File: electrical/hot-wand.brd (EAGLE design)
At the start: 112 x 72 mm, 192 parts, among them IC1 12V R-78K12-2.0, IC2 3V3 R-78K3.3, Q1 STP19NF20, Q2 IRF510, Q3 BC846B, Q4 SIS862ADN-T1-GE3, Q5 2N7002K, Q6 DMTH64M2LPDWQ-13, Q7 SIS862ADN-T1-GE3, Q8 G3404, U1 TPS54560DDA, U2 1EDN8511BXUSA1, U3 INA138, U4 LM74700QDBVTQ1, U5 AP53781, U6 SSD1306-4PIN-0.91N-VERT, U7 STM32F030F4P6, Y1 27.12 MHz 10pF

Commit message: added test points to aid in testing, marks for solder jumpers
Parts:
- added TP1, TP2: TEST-POINT-SQ-2MM, hot-wand:PAD-SQ-2MM
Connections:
- net PWR-ATTENU: now also TP2.1
- net RF-GEN: now also TP1.1
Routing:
- net PWR-ATTENU: track 52.4 -> 55.8 mm
- net RF-GEN: track 58.3 -> 61.0 mm
- net GND: vias 651 -> 652
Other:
- board text added: "A"
- board text added: "B"
- board text added: "C"
- board text added: "D"
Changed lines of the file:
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@@
 </polygon>
 <polygon width="0.2032" layer="32">
-<vertex x="22.8" y="21.6"/>
-<vertex x="24.5" y="21.6"/>
-<vertex x="24.5" y="20.5"/>
-<vertex x="22.8" y="20.5"/>
+<vertex x="21.8" y="21.6"/>
+<vertex x="23.2" y="21.6"/>
+<vertex x="23.2" y="20.4"/>
+<vertex x="21.8" y="20.4"/>
 </polygon>
 <polygon width="0.2032" layer="32">
@@
 <vertex x="90.5" y="65.5"/>
 </polygon>
+<text x="19.2" y="29" size="0.8128" layer="22" font="vector" rot="MR0" align="center">C</text>
+<text x="20.6" y="32.9" size="0.8128" layer="22" font="vector" rot="MR0" align="center">D</text>
+<text x="25" y="20.3" size="0.8128" layer="22" font="vector" rot="MR0" align="center">A</text>
+<text x="20.8" y="21.4" size="0.8128" layer="22" font="vector" rot="MR0" align="center">B</text>
 </plain>
 <attributes>
@@
 </element>
 <element name="L3" library="hot-wand" package="IND_K16X8X6_X2" value="9uH" x="69" y="47" smashed="yes" rot="R270">
-<attribute name="NAME" x="66.9" y="46" size="0.8128" layer="25" font="vector"/>
-<attribute name="VALUE" x="71.3" y="47.9" size="0.8128" layer="27" font="vector" rot="R180"/>
+<attribute name="NAME" x="67" y="44.9" size="0.8128" layer="25" font="vector"/>
+<attribute name="VALUE" x="71.4" y="48.6" size="0.8128" layer="27" font="vector" rot="R180"/>
 <attribute name="JLC-DNP" value="1" x="69" y="47" size="1.778" layer="27" rot="R270" display="off"/>
 </element>
@@
 <attribute name="VALUE" x="40.789" y="50.66" size="0.8128" layer="27" font="vector" ratio="10"/>
 <attribute name="JLC-DNP" value="1" x="45" y="47" size="1.778" layer="27" display="off"/>
+<attribute name="NOTE" value="22 µH fitted; 33 µH original/preferred; 13 µH calculated minimum" x="45" y="47" size="1.778" layer="27" display="off"/>
 </element>
 <element name="L2" library="hot-wand" package="IND_IHLP-2525CZ_VIS-M" value="4u7 IHLP2525CZ" x="55" y="41.4" smashed="yes" rot="MR180">
@@
 <attribute name="NAME" x="92.6" y="66.1" size="0.8128" layer="26" font="fixed" rot="MR90"/>
 </element>
-<element name="FAN1" library="hot-wand" package="FAN-CONN-X4" value="FAN-CONN-X4-CONN-X4" x="23" y="27" smashed="yes" rot="R180"/>
+<element name="FAN1" library="hot-wand" package="FAN-CONN-X4" value="FAN-CONN-X4-CONN-X4" x="23" y="27" smashed="yes" rot="R180">
+<attribute name="PARTNUM" value="WM9797-ND;0470533000" x="23" y="27" size="0.8128" layer="27" font="vector" rot="R180" align="center" display="off"/>
+</element>
 <element name="SJ4" library="hot-wand" package="SJ_3" value="" x="23" y="21" smashed="yes" rot="MR0">
 <attribute name="NAME" x="22.43" y="19.73" size="0.8128" layer="26" rot="MR180"/>
@@
 <attribute name="VALUE" x="20.7" y="30.6999" size="0.02" layer="28" rot="MR90"/>
 <attribute name="VALUE" x="18.795" y="29.53" size="0.4064" layer="28" rot="MR90"/>
+</element>
+<element name="TP1" library="hot-wand" package="PAD-SQ-2MM" value="TEST-POINT-SQ-2MM" x="47.3" y="20.9" smashed="yes">
+<attribute name="NAME" x="46" y="22.3" size="0.8128" layer="25"/>
+</element>
+<element name="TP2" library="hot-wand" package="PAD-SQ-2MM" value="TEST-POINT-SQ-2MM" x="50.6" y="18.8" smashed="yes">
+<attribute name="NAME" x="50.2" y="20.2" size="0.8128" layer="25"/>
 </element>
 </elements>
@@
 <via x="70.5" y="52.1" extent="1-16" drill="0.3" shape="octagon"/>
 <via x="70.4" y="49" extent="1-16" drill="0.3" shape="octagon"/>
-<via x="75.2" y="46" extent="1-16" drill="0.3" shape="octagon"/>
 <via x="71.4" y="45" extent="1-16" drill="0.3" shape="octagon"/>
 <via x="63" y="45" extent="1-16" drill="0.3" shape="octagon"/>
 <via x="60" y="45" extent="1-16" drill="0.3" shape="octagon"/>
 <via x="67" y="49" extent="1-16" drill="0.3" shape="octagon"/>
-<via x="67.4" y="46" extent="1-16" drill="0.3" shape="octagon"/>
 <via x="67.4" y="44" extent="1-16" drill="0.3" shape="octagon"/>
 <via x="67.4" y="42" extent="1-16" drill="0.3" shape="octagon"/>
@@
 <via x="38" y="17.2" extent="1-16" drill="0.3" shape="octagon"/>
 <via x="38" y="13.8" extent="1-16" drill="0.3" shape="octagon"/>
-<via x="46.7" y="19.3" extent="1-16" drill="0.3" shape="octagon"/>
+<via x="46.2" y="19.1" extent="1-16" drill="0.3" shape="octagon"/>
 <via x="45.8" y="15.2" extent="1-16" drill="0.3" shape="octagon"/>
 <via x="45.8" y="13.8" extent="1-16" drill="0.3" shape="octagon"/>
@@
 <via x="54" y="30" extent="1-16" drill="0.3" shape="octagon"/>
 <via x="50" y="33" extent="1-16" drill="0.3" shape="octagon"/>
-<via x="44" y="36" extent="1-16" drill="0.3" shape="octagon"/>
+<via x="44" y="35.4" extent="1-16" drill="0.3" shape="octagon"/>
 <via x="44" y="34" extent="1-16" drill="0.3" shape="octagon"/>
 <via x="13" y="24" extent="1-16" drill="0.3" shape="octagon"/>
@@
 <via x="54.5" y="58" extent="1-16" drill="0.3" shape="octagon"/>
 <via x="56" y="58" extent="1-16" drill="0.3" shape="octagon"/>
-<via x="63.5" y="68.9" extent="1-16" drill="0.3" shape="octagon"/>
+<via x="63.54" y="68.9" extent="1-16" drill="0.3" shape="octagon"/>
 <contactref element="C61" pad="C"/>
 <contactref element="SJ4" pad="1"/>
@@
 <via x="26.8" y="30.1" extent="1-16" drill="0.3" shape="octagon"/>
 <via x="24.8" y="30.1" extent="1-16" drill="0.3" shape="octagon"/>
-<via x="25.8" y="20.9" extent="1-16" drill="0.3" shape="octagon"/>
+<via x="25.8" y="21" extent="1-16" drill="0.3" shape="octagon"/>
 <via x="27.2" y="22.5" extent="1-16" drill="0.3" shape="octagon"/>
 <via x="23.9" y="19.8" extent="1-16" drill="0.3" shape="octagon"/>
@@
 <via x="101" y="62.9" extent="1-16" drill="0.3" shape="octagon"/>
 <via x="101" y="59.7" extent="1-16" drill="0.3" shape="octagon"/>
+<via x="75.1" y="44.7" extent="1-16" drill="1" diameter="2" shape="octagon" alwaysstop="yes"/>
+<via x="68" y="47" extent="1-16" drill="1" diameter="2" shape="octagon" alwaysstop="yes"/>
+<via x="24.8" y="21" extent="1-16" drill="0.3" shape="octagon"/>
 </signal>
 <signal name="RF-OUT">
@@
 <wire x1="48.2" y1="27.2" x2="45.4" y2="30" width="0.2032" layer="1"/>
 <wire x1="45.4" y1="30" x2="43.1" y2="30" width="0.2032" layer="1"/>
-<wire x1="38.8" y1="48.2" x2="42.7" y2="52.1" width="0.2032" layer="1"/>
-<wire x1="42.7" y1="52.1" x2="42.7" y2="57.7" width="0.2032" layer="1"/>
+<wire x1="38.8" y1="48.4" x2="42.7" y2="52.3" width="0.2032" layer="1"/>
+<wire x1="42.7" y1="52.3" x2="42.7" y2="57.7" width="0.2032" layer="1"/>
 <wire x1="42.7" y1="57.7" x2="44" y2="59" width="0.2032" layer="1"/>
 <wire x1="44" y1="59" x2="44" y2="67.4" width="0.2032" layer="1"/>
 <via x="44" y="67.4" extent="1-16" drill="0.3" shape="octagon"/>
-<wire x1="38.8" y1="34.3" x2="38.8" y2="48.2" width="0.2032" layer="1"/>
+<wire x1="38.8" y1="34.3" x2="38.8" y2="48.4" width="0.2032" layer="1"/>
 <wire x1="38.8" y1="34.3" x2="43.1" y2="30" width="0.2032" layer="1"/>
 <wire x1="44" y1="67.4" x2="44" y2="68.9" width="0.4064" layer="16"/>
 <contactref element="R52" pad="2"/>
 <wire x1="48.2" y1="18" x2="48.2" y2="19.1" width="0.4064" layer="16"/>
+<contactref element="TP1" pad="1"/>
+<wire x1="47.3" y1="20.9" x2="48.2" y2="20.9" width="0.2032" layer="1"/>
+<wire x1="48.2" y1="20.9" x2="48.2" y2="19.1" width="0.2032" layer="1"/>
 </signal>
 <signal name="N$28">
@@
 <wire x1="49.7" y1="27.698334375" x2="46.098334375" y2="31.3" width="0.2032" layer="1"/>
 <wire x1="46.098334375" y1="31.3" x2="43.5" y2="31.3" width="0.2032" layer="1"/>
-<wire x1="39.9" y1="34.9" x2="39.9" y2="47.7" width="0.2032" layer="1"/>
-<wire x1="39.9" y1="47.7" x2="44.2" y2="52" width="0.2032" layer="1"/>
-<via x="44.2" y="52" extent="1-16" drill="0.3" shape="octagon"/>
-<wire x1="44.2" y1="52" x2="45.35" y2="52" width="0.4064" layer="16"/>
-<wire x1="45.35" y1="52" x2="46.6" y2="53.25" width="0.4064" layer="16"/>
+<wire x1="39.9" y1="34.9" x2="39.9" y2="47.8" width="0.2032" layer="1"/>
+<wire x1="39.9" y1="47.8" x2="44.2" y2="52.1" width="0.2032" layer="1"/>
+<via x="44.2" y="52.1" extent="1-16" drill="0.3" shape="octagon"/>
+<wire x1="44.2" y1="52.1" x2="45.45" y2="52.1" width="0.4064" layer="16"/>
+<wire x1="45.45" y1="52.1" x2="46.6" y2="53.25" width="0.4064" layer="16"/>
 <via x="49.7" y="16.4" extent="1-16" drill="0.3" shape="octagon"/>
 <wire x1="39.9" y1="34.9" x2="43.5" y2="31.3" width="0.2032" layer="1"/>
+<contactref element="TP2" pad="1"/>
+<wire x1="50.6" y1="18.8" x2="49.7" y2="18.8" width="0.2032" layer="1"/>
+<wire x1="49.7" y1="18.8" x2="49.7" y2="16.4" width="0.2032" layer="1"/>
 </signal>
 <signal name="12V-2">

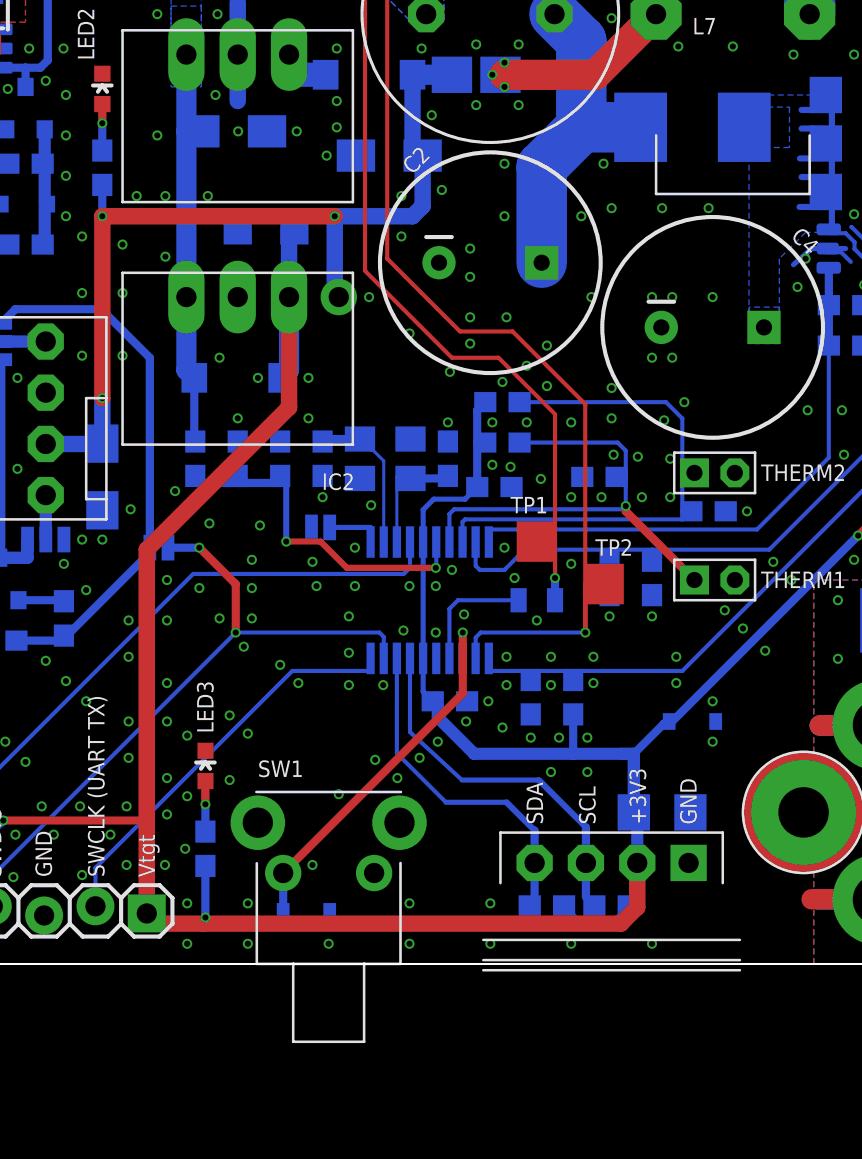
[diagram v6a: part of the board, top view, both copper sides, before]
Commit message: moved the oled, 3.3V buck converter footprint fixed
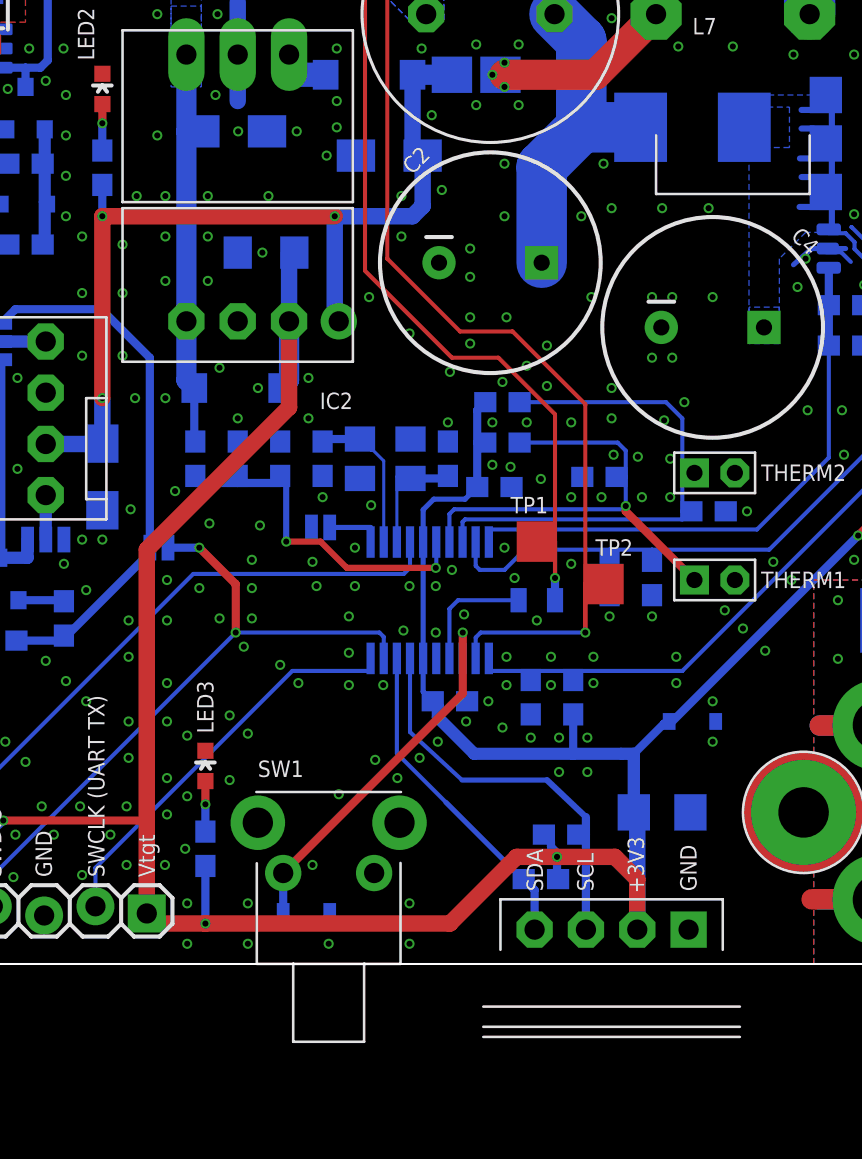
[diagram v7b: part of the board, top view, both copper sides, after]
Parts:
- IC1: device hot-wand:TO220-BUCK -> hot-wand:TO220-BUCK-12V
- IC2: device hot-wand:TO220-BUCK -> hot-wand:TO220-BUCK-3.3V
- moved R36 4.30 mm to (48.5, 6.40), turned to 0 degrees
- moved U6 3.30 mm to (51.0, 1.70)
- moved R35 1.33 mm to (47.5, 4.20)
- moved IC2 1.20 mm to (32.5, 31.8)
- moved C45 1.20 mm to (33.9, 35.2)
- moved D11 0.50 mm to (32.5, 28.5)
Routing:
- net SCL: track 18.3 -> 20.0 mm
- net +12V: track 44.7 -> 45.9 mm
- net SDA: track 17.0 -> 16.3 mm
- net 3.3V: track 140.9 -> 140.4 mm, vias 3 -> 4
- net GND: vias 652 -> 655

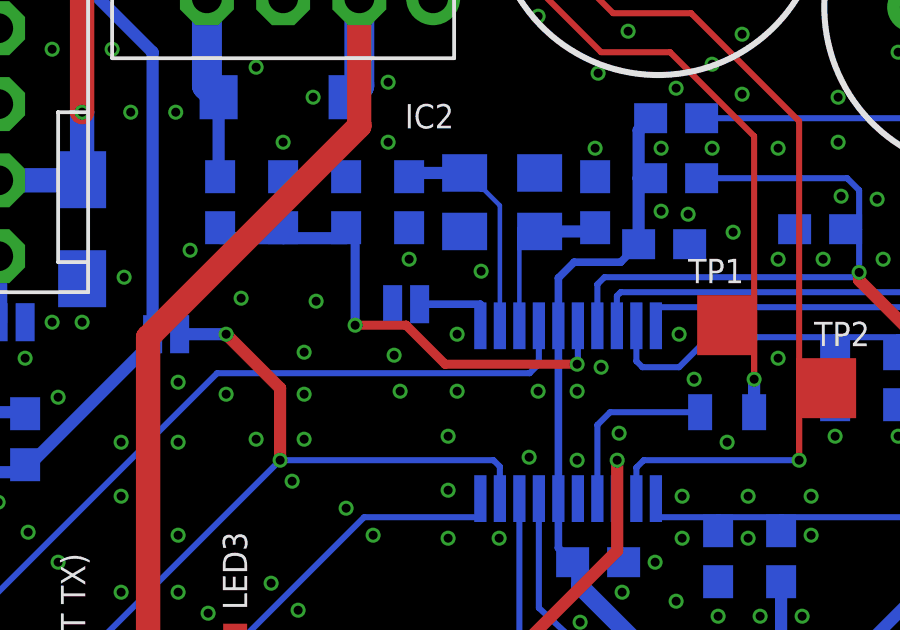
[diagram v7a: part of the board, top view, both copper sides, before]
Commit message: BOOT0 trace thicker
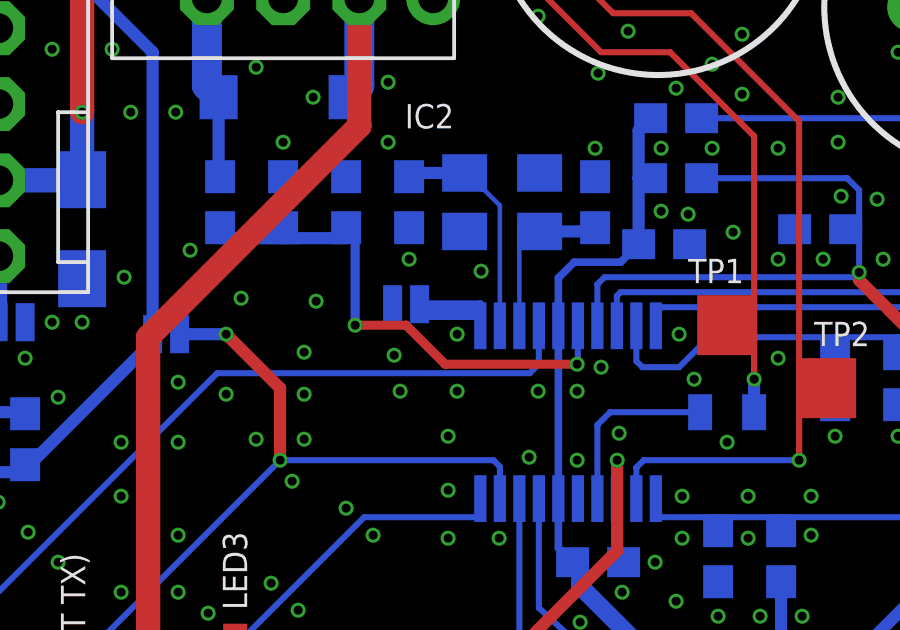
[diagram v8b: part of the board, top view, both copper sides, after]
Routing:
- net N$26: track 2.75 -> 6.80 mm
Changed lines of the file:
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@@
 <contactref element="U7" pad="1"/>
 <contactref element="SJ1" pad="2"/>
-<wire x1="39.075" y1="20.88" x2="39.075" y2="21.6" width="0.254" layer="16"/>
+<wire x1="39.075" y1="20.88" x2="39.075" y2="21.2" width="0.254" layer="16"/>
+<wire x1="39.075" y1="21.2" x2="39.075" y2="21.4" width="0.254" layer="16"/>
+<wire x1="39.075" y1="21.4" x2="39.075" y2="21.6" width="0.254" layer="16"/>
 <wire x1="39.075" y1="21.6" x2="37.05" y2="21.6" width="0.254" layer="16"/>
+<wire x1="39.075" y1="21.4" x2="37.05" y2="21.4" width="0.254" layer="16"/>
+<wire x1="39.075" y1="21.2" x2="37.05" y2="21.2" width="0.254" layer="16"/>
 </signal>
 <signal name="N$50">
